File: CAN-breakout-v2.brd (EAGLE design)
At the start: 27.9 x 15.2 mm, 10 parts, among them IC1 TJA1049

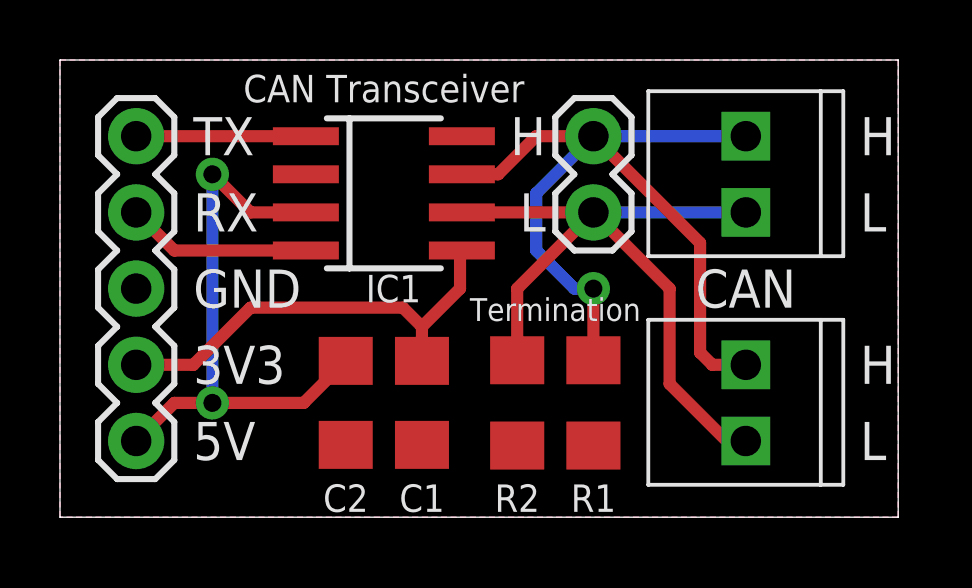
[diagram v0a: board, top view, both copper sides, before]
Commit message: Fix the termination
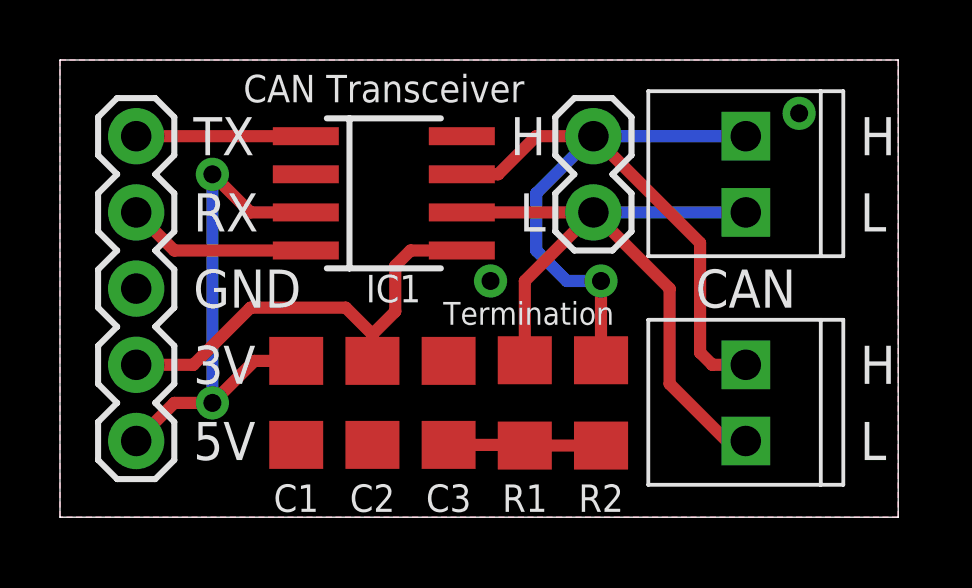
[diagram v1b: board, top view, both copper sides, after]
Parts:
- added C3: 0.01u, rcl:C1206
- R1, R2: value 60 -> 62
- moved C1 4.19 mm to (7.87, 3.81)
- moved R2 2.79 mm to (18.0, 3.81)
- moved R1 2.29 mm to (15.5, 3.81)
- moved C2 0.89 mm to (10.4, 3.81)
- moved U$3 0.25 mm to (9.70, 3.35)
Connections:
- new net N$7: C3.2, R1.1, R2.1
- net 3.3V: now also C2.2; no longer C1.2
- net 5V: now also C1.2; no longer C2.2
- net CANH: now also R2.2; no longer R1.2
- net CANL: now also R1.2; no longer R2.2
- net GND: now also C3.1; no longer R1.1, R2.1
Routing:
- net N$7: track 0.00 -> 5.10 mm
- net 5V: track 19.4 -> 17.7 mm
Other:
- board text added: "3V"
- board text added: "Particle wiring: RX=D2, TX=D1, 3V=3V3, 5V=VIN, GND=GND"
- board text added: "Screw terminals are the same bus Solder R1=R2=62 at ends of bus"
- board text added: "V2"
- board text removed: "3V3"
- board text removed: "Particle wiring: RX=D2, TX=D1, 3V3=3V3, 5V=VIN, GND=GND"
- board text removed: "Screw terminals are the same bus Solder R1=R2=60 at ends of bus"
- board text removed: "V1"
